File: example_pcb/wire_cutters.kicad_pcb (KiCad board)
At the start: 2 copper layers, 45.4 x 12.4 mm, 9 parts, among them J1 Conn_01x02, J2 Conn_01x03, J3 Conn_01x03, Q1 2SCR293P, Q2 IRF-100S201

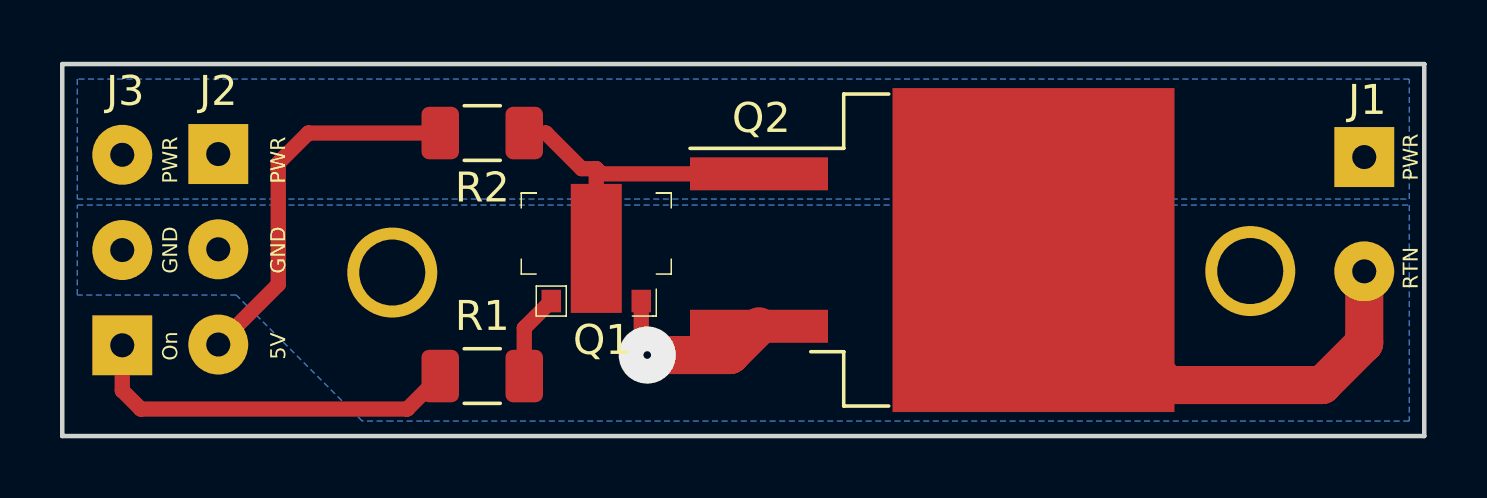
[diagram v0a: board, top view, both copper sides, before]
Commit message: Removed the N-Channel Resistor from the schematic, netlist, and layout to be added as an example in lecture.
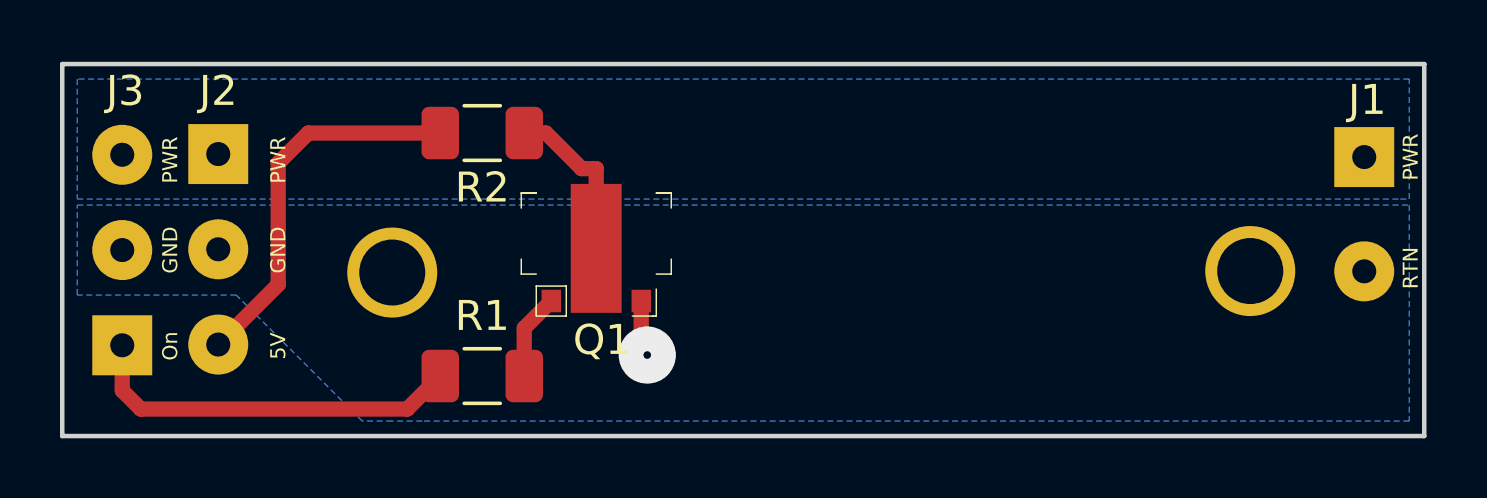
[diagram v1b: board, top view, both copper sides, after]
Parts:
- removed Q2: IRF-100S201, Package_TO_SOT_SMD:TO-263-2
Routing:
- net Net-(J1-Pad2): track 20.3 -> 0.00 mm
- net Net-(Q1-Pad2): track 12.3 -> 6.85 mm
- net GND: track 6.01 -> 1.88 mm
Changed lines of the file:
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@@
     (thickness 0.8)
     (drawings 12)
-    (tracks 28)
+    (tracks 18)
     (zones 0)
-    (modules 9)
+    (modules 8)
     (nets 8)
   )
@@
     (46 B.CrtYd user)
     (47 F.CrtYd user)
-    (49 F.Fab user hide)
+    (49 F.Fab user)
   )
   (setup
@@
       (net 5 Batt_Raw))
   )
-  (module Package_TO_SOT_SMD:TO-263-2 (layer F.Cu)
-    (at 177 100)
-    (descr "TO-263 / D2PAK / DDPAK SMD package, http://www.infineon.com/cms/en/product/packages/PG-TO263/PG-TO263-3-1/")
-    (tags "D2PAK DDPAK TO-263 D2PAK-3 TO-263-3 SOT-404")
-    (attr smd)
-    (fp_text reference Q2 (at -5.7 -4.4 180) (layer F.SilkS)
-      (effects (font (size 1 1) (thickness 0.15)))
-    )
-    (fp_text value IRF-100S201 (at 0 6.65) (layer F.Fab)
-      (effects (font (size 1 1) (thickness 0.15)))
-    )
-    (fp_line (start 6.5 -5) (end 7.5 -5) (layer F.Fab) (width 0.1))
-    (fp_line (start 7.5 -5) (end 7.5 5) (layer F.Fab) (width 0.1))
-    (fp_line (start 7.5 5) (end 6.5 5) (layer F.Fab) (width 0.1))
-    (fp_line (start 6.5 -5) (end 6.5 5) (layer F.Fab) (width 0.1))
-    (fp_line (start 6.5 5) (end -2.75 5) (layer F.Fab) (width 0.1))
-    (fp_line (start -2.75 5) (end -2.75 -4) (layer F.Fab) (width 0.1))
-    (fp_line (start -2.75 -4) (end -1.75 -5) (layer F.Fab) (width 0.1))
-    (fp_line (start -1.75 -5) (end 6.5 -5) (layer F.Fab) (width 0.1))
-    (fp_line (start -2.75 -3.04) (end -7.45 -3.04) (layer F.Fab) (width 0.1))
-    (fp_line (start -7.45 -3.04) (end -7.45 -2.04) (layer F.Fab) (width 0.1))
-    (fp_line (start -7.45 -2.04) (end -2.75 -2.04) (layer F.Fab) (width 0.1))
-    (fp_line (start -2.75 2.04) (end -7.45 2.04) (layer F.Fab) (width 0.1))
-    (fp_line (start -7.45 2.04) (end -7.45 3.04) (layer F.Fab) (width 0.1))
-    (fp_line (start -7.45 3.04) (end -2.75 3.04) (layer F.Fab) (width 0.1))
-    (fp_line (start -1.45 -5.2) (end -2.95 -5.2) (layer F.SilkS) (width 0.12))
-    (fp_line (start -2.95 -5.2) (end -2.95 -3.39) (layer F.SilkS) (width 0.12))
-    (fp_line (start -2.95 -3.39) (end -8.075 -3.39) (layer F.SilkS) (width 0.12))
-    (fp_line (start -1.45 5.2) (end -2.95 5.2) (layer F.SilkS) (width 0.12))
-    (fp_line (start -2.95 5.2) (end -2.95 3.39) (layer F.SilkS) (width 0.12))
-    (fp_line (start -2.95 3.39) (end -4.05 3.39) (layer F.SilkS) (width 0.12))
-    (fp_line (start -8.32 -5.65) (end -8.32 5.65) (layer F.CrtYd) (width 0.05))
-    (fp_line (start -8.32 5.65) (end 8.32 5.65) (layer F.CrtYd) (width 0.05))
-    (fp_line (start 8.32 5.65) (end 8.32 -5.65) (layer F.CrtYd) (width 0.05))
-    (fp_line (start 8.32 -5.65) (end -8.32 -5.65) (layer F.CrtYd) (width 0.05))
-    (fp_text user %R (at 0 0) (layer F.Fab)
-      (effects (font (size 1 1) (thickness 0.15)))
-    )
-    (pad 1 smd rect (at -5.775 -2.54) (size 4.6 1.1) (layers F.Cu F.Paste F.Mask)
-      (net 3 "Net-(Q1-Pad2)"))
-    (pad 3 smd rect (at -5.775 2.54) (size 4.6 1.1) (layers F.Cu F.Paste F.Mask)
-      (net 1 GND))
-    (pad 2 smd rect (at 3.375 0) (size 9.4 10.8) (layers F.Cu F.Mask)
-      (net 6 "Net-(J1-Pad2)"))
-    (pad "" smd rect (at 5.8 2.775) (size 4.55 5.25) (layers F.Paste))
-    (pad "" smd rect (at 0.95 -2.775) (size 4.55 5.25) (layers F.Paste))
-    (pad "" smd rect (at 5.8 -2.775) (size 4.55 5.25) (layers F.Paste))
-    (pad "" smd rect (at 0.95 2.775) (size 4.55 5.25) (layers F.Paste))
-    (model ${KISYS3DMOD}/Package_TO_SOT_SMD.3dshapes/TO-263-2.wrl
-      (at (xyz 0 0 0))
-      (scale (xyz 1 1 0.7))
-      (rotate (xyz 0 0 0))
-    )
-  )
   (module Resistor_SMD:R_1206_3216Metric (layer F.Cu)
     (at 162 104.2 180)
@@
   (segment (start 167.3 103.3) (end 167.5 103.5) (width 0.508) (layer F.Cu) (net 1))
   (segment (start 167.3 101.7) (end 167.3 103.3) (width 0.508) (layer F.Cu) (net 1) (status 10))
-  (segment (start 170.265 103.5) (end 171.225 102.54) (width 1.27) (layer F.Cu) (net 1) (status 20))
-  (segment (start 167.5 103.5) (end 170.265 103.5) (width 1.27) (layer F.Cu) (net 1))
   (segment (start 163.4 102.6) (end 164.3 101.7) (width 0.508) (layer F.Cu) (net 2) (status 20))
   (segment (start 163.4 102.6) (end 163.4 104.2) (width 0.508) (layer F.Cu) (net 2) (status 20))
@@
   (segment (start 165.8 99.945) (end 165.8 97.287) (width 0.508) (layer F.Cu) (net 3) (status 10))
   (segment (start 165.312 97.287) (end 165.8 97.287) (width 0.508) (layer F.Cu) (net 3))
-  (segment (start 165.973 97.46) (end 165.8 97.287) (width 0.508) (layer F.Cu) (net 3))
-  (segment (start 171.225 97.46) (end 165.973 97.46) (width 0.508) (layer F.Cu) (net 3) (status 10))
   (segment (start 159.5 105.3) (end 160.6 104.2) (width 0.508) (layer F.Cu) (net 4) (status 20))
   (segment (start 150.61751 105.3) (end 159.5 105.3) (width 0.508) (layer F.Cu) (net 4))
   (segment (start 150 103.175) (end 150 104.68249) (width 0.508) (layer F.Cu) (net 4) (status 10))
   (segment (start 150 104.68249) (end 150.61751 105.3) (width 0.508) (layer F.Cu) (net 4))
-  (segment (start 182.385 100.71) (end 181.675 100) (width 1.27) (layer F.Cu) (net 6) (status 30))
-  (segment (start 182.81322 102.43822) (end 180.375 100) (width 1.27) (layer F.Cu) (net 6) (status 30))
-  (segment (start 191.4 100.71) (end 191.4 103.1) (width 1.27) (layer F.Cu) (net 6) (status 10))
-  (segment (start 191.4 103.1) (end 190 104.5) (width 1.27) (layer F.Cu) (net 6))
-  (segment (start 184.875 104.5) (end 180.375 100) (width 1.27) (layer F.Cu) (net 6) (status 30))
-  (segment (start 190 104.5) (end 184.875 104.5) (width 1.27) (layer F.Cu) (net 6) (status 20))
   (segment (start 156.2 96.1) (end 160.6 96.1) (width 0.508) (layer F.Cu) (net 7) (status 20))
   (segment (start 155.2 97.1) (end 156.2 96.1) (width 0.508) (layer F.Cu) (net 7))
